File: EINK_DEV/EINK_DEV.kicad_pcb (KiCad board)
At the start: 4 copper layers, 76.2 x 50.7 mm, 80 parts, among them J1 FPC, J2 UART1, J3 Conn_01x02, J4 Conn_01x03, J5 Conn_ARM_SWD_TagConnect_TC2030, J6 LOW POWER UART, J7 Conn_Coaxial, J8 USER1, J9 USER2, P1 USB_C_Plug_USB2.0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

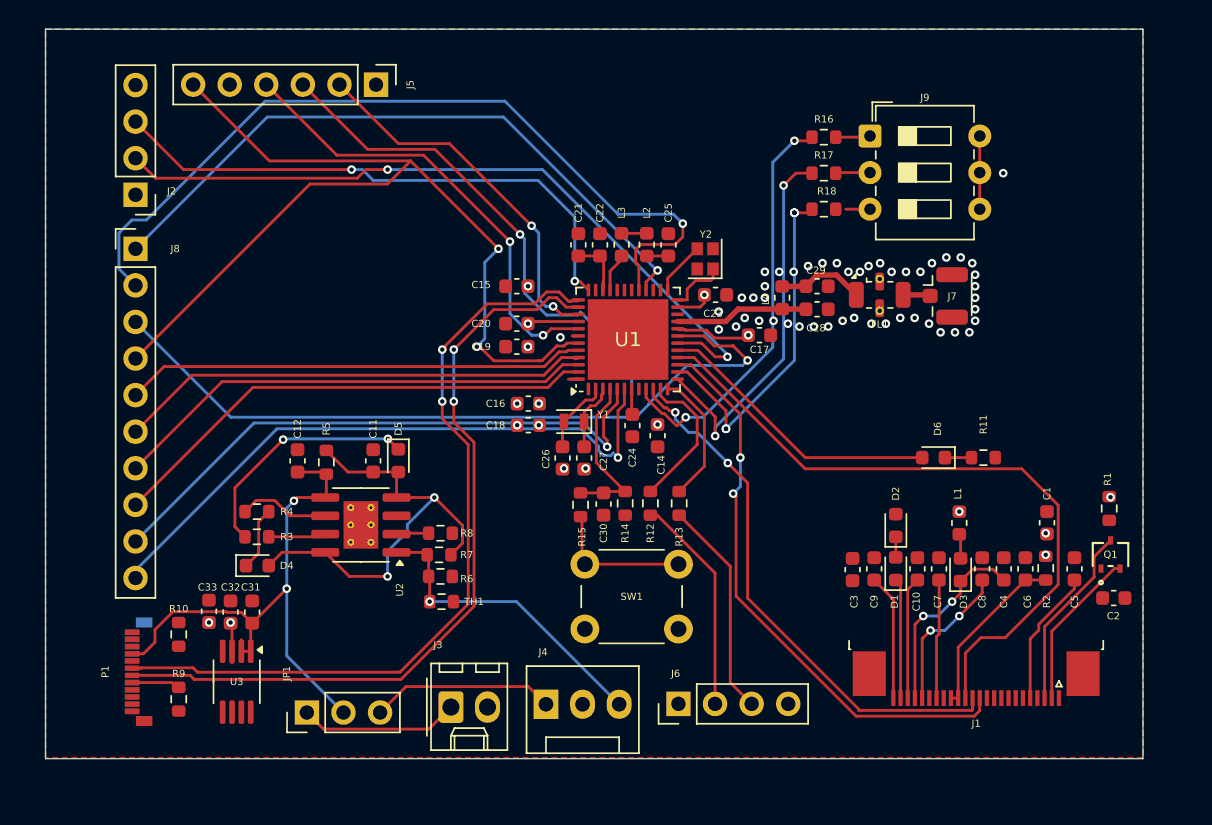
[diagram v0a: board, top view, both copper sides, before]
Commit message: Final changes
Fixed RF shape
Fixed USB C conn
Fixed a lot of DRCs
Fixed broken Footprints
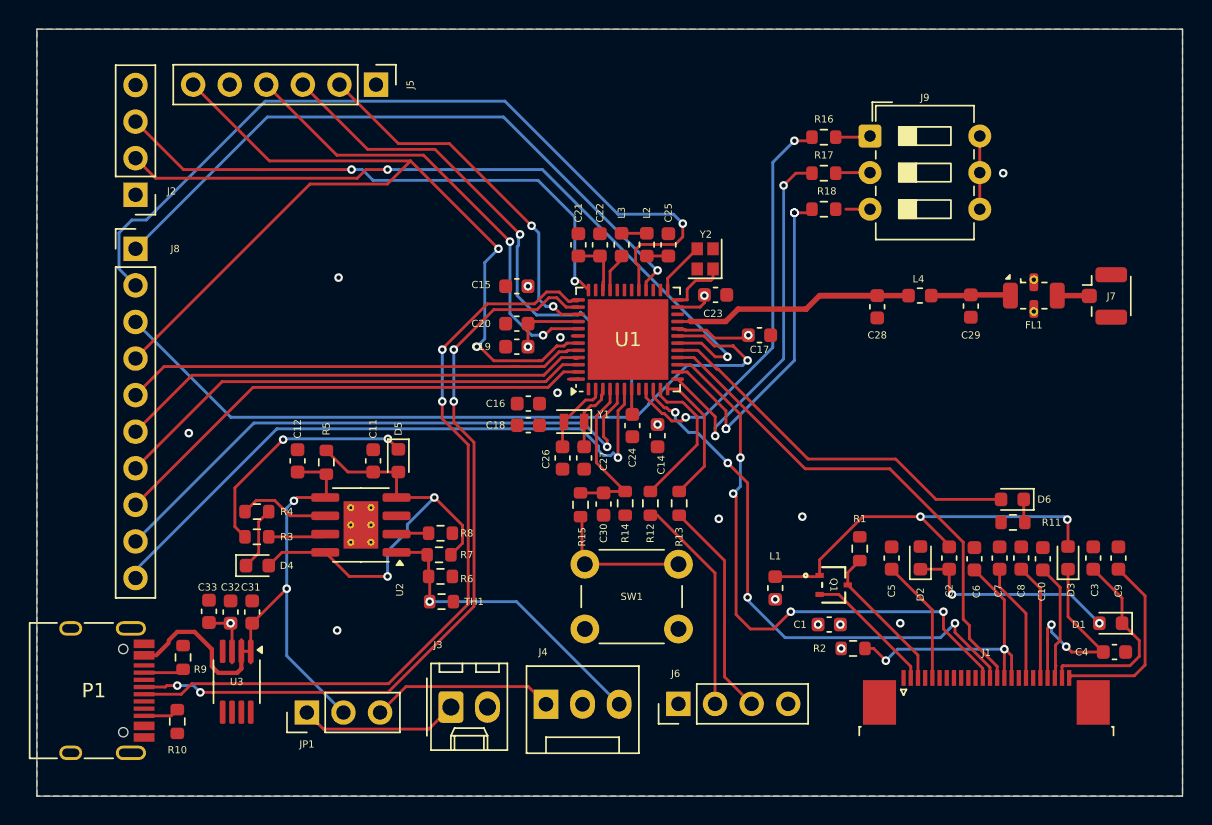
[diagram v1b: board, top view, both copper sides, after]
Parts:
- P1: footprint Connector_USB:USB_C_Plug_Molex_105444 -> Connector_USB:USB_C_Receptacle_HRO_TYPE-C-31-M-12
- moved Q1 19.3 mm to (112.0, 92.3), turned to -90 degrees
- moved R1 17.5 mm to (113.8, 89.8)
- moved C9 17.0 mm to (131.8, 90.5)
- moved C3 16.7 mm to (130.0, 90.5)
- moved C1 16.7 mm to (111.7, 95.1), turned to 180 degrees
- moved D1 15.4 mm to (131.2, 95.0), turned to 180 degrees
- moved R2 14.5 mm to (113.3, 96.8), turned to 0 degrees
- moved L1 13.6 mm to (107.9, 92.6), turned to 90 degrees
- moved C5 12.7 mm to (116.0, 90.5)
- moved C2 11.8 mm to (120.0, 90.5), turned to 90 degrees
- moved J7 11.1 mm to (130.8, 72.3)
- moved C29 10.8 mm to (121.5, 73.0), turned to -90 degrees
- moved FL1 10.7 mm to (125.9, 72.2)
- moved C4 9.61 mm to (131.5, 97.0), turned to 180 degrees
- moved L4 9.56 mm to (118.0, 72.2), turned to 0 degrees
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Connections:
- SW1 pad 2: +3V3 -> +3.3V
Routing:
- net Net-(D3-A): track 1.71 -> 27.5 mm, vias 0 -> 2
- net Net-(D1-A): track 1.42 -> 14.9 mm, vias 0 -> 2
- net SDA_SCREEN: track 47.7 -> 35.6 mm
- net RF_sub: track 9.27 -> 20.8 mm
- net Net-(J1-Pin_15): track 12.1 -> 20.8 mm, vias 0 -> 2
- net Net-(D6-A): track 20.1 -> 26.7 mm
- net VGL: track 8.34 -> 13.8 mm
- net VCOM: track 8.75 -> 13.1 mm
- net +3V3: track 20.7 -> 23.8 mm, vias 14 -> 10
- net VSH: track 10.9 -> 8.10 mm, vias 2 -> 0
- net Net-(P1-VCONN): track 0.00 -> 2.48 mm
- net RESE: track 12.8 -> 10.5 mm
- net GDR: track 11.2 -> 9.20 mm
- net VGH: track 13.7 -> 15.5 mm
- net VBUS: track 39.8 -> 41.2 mm
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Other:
- board size 76.2 x 50.7 mm -> 79.5 x 53.3 mm

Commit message: Ostateczny commit chyba
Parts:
- moved C24 0.90 mm to (98.0, 82.2)
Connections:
- SW1 pad 2: +3.3V -> +3V3
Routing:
- net GND: track 0.00 -> 44.4 mm, vias 8 -> 21
- net unconnected-(P1-SHIELD-PadS1): track 0.00 -> 17.0 mm
- net +3V3: track 23.8 -> 32.5 mm, vias 10 -> 8
- net VBUS: track 41.2 -> 48.3 mm
- net VGL: track 13.8 -> 15.7 mm
- net SWD_NRST: track 38.5 -> 39.8 mm, vias 1 -> 2
- net Net-(J8-Pin_3): track 52.6 -> 53.8 mm
- net VCOM: track 13.1 -> 13.9 mm
- net Net-(J8-Pin_10): track 44.2 -> 44.9 mm
- net Net-(J9-Pad3): track 1.43 -> 2.13 mm
- net Net-(D5-K): track 16.8 -> 17.3 mm
